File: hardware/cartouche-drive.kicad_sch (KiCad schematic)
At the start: 70 parts, among them J1 USB-C 105450-0101, J2 M.2 key M (2230), U1 JMS583, U2 TPS82130, U3 ZD25WQ16, Y1 25MHz 12pF

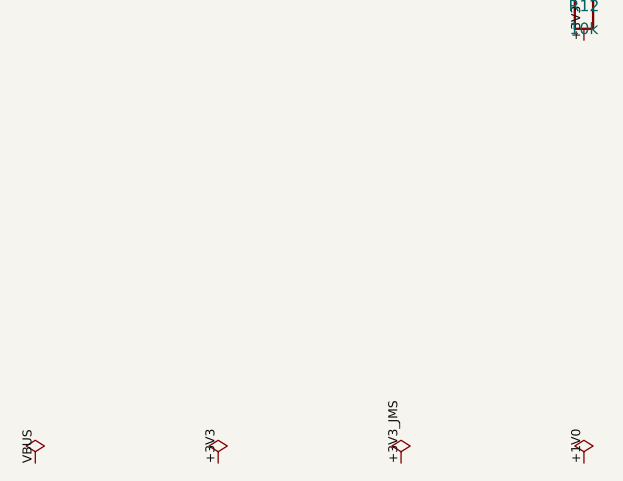
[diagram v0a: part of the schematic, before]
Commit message: PCB draft v0.1: placement, 4-layer planes, fan-out vias (not for fab)
30 x 66 mm, 4 layers: In1 solid GND, In2 split VBUS / +3V3 (SSD).
Parts placed next to the pin they serve; SSD 3.3 V buck under the SSD.
Freerouting draft: schematic parity 0, 18 unconnected left.
The 10 Gb/s USB and PCIe pairs must be re-routed as coupled pairs.

Co-Authored-By: Claude Opus 5.5 <noreply@anthropic.com>
Claude-Session: https://claude.ai/code/session_01RqDGjrUG4GdEsawKGChjmB
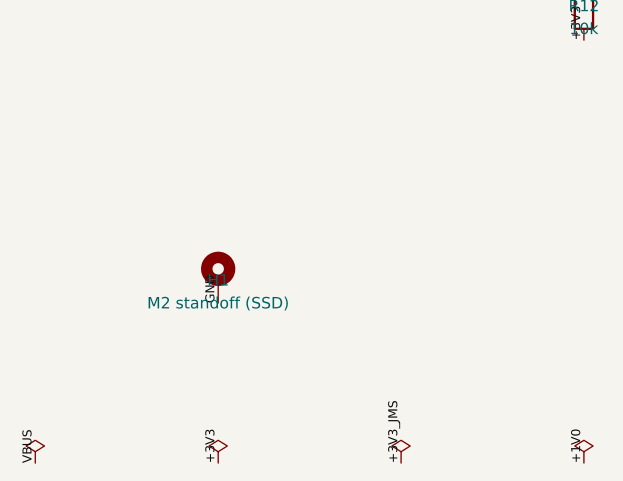
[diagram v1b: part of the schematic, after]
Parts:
- added H1: M2 standoff (SSD), MountingHole:MountingHole_2.2mm_M2_Pad_Via, symbol Mechanical:MountingHole_Pad
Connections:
- net GND: now also H1.1
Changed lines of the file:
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@@
     (pin "2")
     (instances (project "cartouche-drive" (path "/d24663b6-b77d-57d9-a649-cdccb3ccec1d" (reference "C46") (unit 1)))))
+  (symbol (lib_id "Mechanical:MountingHole_Pad") (at 59.69 330.2 0) (unit 1) (exclude_from_sim no) (in_bom no) (on_board yes) (dnp no)
+    (property "Reference" "H1" (at 59.69 330.2 0) (effects (font (size 1.27 1.27))))
+    (property "Value" "M2 standoff (SSD)" (at 59.69 332.74 0) (effects (font (size 1.27 1.27))))
+    (property "Footprint" "MountingHole:MountingHole_2.2mm_M2_Pad_Via" (at 59.69 335.28 0) (effects (font (size 1.27 1.27)) (hide yes)))
+    (property "Datasheet" "" (at 59.69 337.82 0) (effects (font (size 1.27 1.27)) (hide yes)))
+    (property "LCSC" "" (at 59.69 340.36 0) (effects (font (size 1.27 1.27)) (hide yes)))
+    (pin "1")
+    (instances (project "cartouche-drive" (path "/d24663b6-b77d-57d9-a649-cdccb3ccec1d" (reference "H1") (unit 1)))))
   (symbol (lib_id "power:PWR_FLAG") (at 39.37 350.52 0) (unit 1) (exclude_from_sim no) (in_bom no) (on_board no) (dnp no)
     (property "Reference" "#FLG1" (at 39.37 350.52 0) (effects (font (size 1.27 1.27)) (hide yes)))
@@
   (label "+3V3" (at 389.89 106.68 90) (effects (font (size 1.0 1.0)) (justify left bottom)))
   (label "GND" (at 389.89 114.3 270) (effects (font (size 1.0 1.0)) (justify left bottom)))
+  (label "GND" (at 59.69 332.74 270) (effects (font (size 1.0 1.0)) (justify left bottom)))
   (label "VBUS" (at 39.37 350.52 270) (effects (font (size 1.0 1.0)) (justify left bottom)))
   (label "+3V3" (at 59.69 350.52 270) (effects (font (size 1.0 1.0)) (justify left bottom)))

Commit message: PCB v0.2 WIP: fix PCIe TX/RX to M.2, new layout, scripted PCIe pairs
Schematic fix: M.2 PCIe pins are named from the host side (PET = host TX).
Our TX now goes through the 220 nF caps to PET0/PET1, RX comes from PER0/PER1.

New 36 x 46 mm layout: JMS583 under the SSD, its PCIe side facing the
socket's PCIe pins in the same order; USB-C on the left edge.
The 5 PCIe pairs are routed by the script (straight, one jog, caps staggered),
1.0 V and REXT pins on that side escape to vias inside the pin ring.
Still to do: USB 3.2 pairs (B-row vias between the two rows), power pours.
Not for fabrication yet.

Co-Authored-By: Claude Opus 5.5 <noreply@anthropic.com>
Claude-Session: https://claude.ai/code/session_01RqDGjrUG4GdEsawKGChjmB
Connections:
- net PCIE_RXN0: now also J2.41; no longer J2.47
- net PCIE_RXN1: now also J2.29; no longer J2.35
- net PCIE_RXP0: now also J2.43; no longer J2.49
- net PCIE_RXP1: now also J2.31; no longer J2.37
- net PCIE_TXN0_M2: now also J2.47; no longer J2.41
- net PCIE_TXN1_M2: now also J2.35; no longer J2.29
- net PCIE_TXP0_M2: now also J2.49; no longer J2.43
- net PCIE_TXP1_M2: now also J2.37; no longer J2.31
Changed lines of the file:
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@@
   (label "REFCLK_N" (at 322.58 168.91 180) (effects (font (size 1.0 1.0)) (justify right bottom)))
   (label "GND" (at 322.58 166.37 180) (effects (font (size 1.0 1.0)) (justify right bottom)))
-  (label "PCIE_RXP0" (at 322.58 163.83 180) (effects (font (size 1.0 1.0)) (justify right bottom)))
-  (label "PCIE_RXN0" (at 322.58 161.29 180) (effects (font (size 1.0 1.0)) (justify right bottom)))
+  (label "PCIE_TXP0_M2" (at 322.58 163.83 180) (effects (font (size 1.0 1.0)) (justify right bottom)))
+  (label "PCIE_TXN0_M2" (at 322.58 161.29 180) (effects (font (size 1.0 1.0)) (justify right bottom)))
   (label "GND" (at 322.58 158.75 180) (effects (font (size 1.0 1.0)) (justify right bottom)))
-  (label "PCIE_TXP0_M2" (at 322.58 156.21 180) (effects (font (size 1.0 1.0)) (justify right bottom)))
-  (label "PCIE_TXN0_M2" (at 322.58 153.67 180) (effects (font (size 1.0 1.0)) (justify right bottom)))
+  (label "PCIE_RXP0" (at 322.58 156.21 180) (effects (font (size 1.0 1.0)) (justify right bottom)))
+  (label "PCIE_RXN0" (at 322.58 153.67 180) (effects (font (size 1.0 1.0)) (justify right bottom)))
   (label "GND" (at 322.58 151.13 180) (effects (font (size 1.0 1.0)) (justify right bottom)))
-  (label "PCIE_RXP1" (at 322.58 148.59 180) (effects (font (size 1.0 1.0)) (justify right bottom)))
-  (label "PCIE_RXN1" (at 322.58 146.05 180) (effects (font (size 1.0 1.0)) (justify right bottom)))
+  (label "PCIE_TXP1_M2" (at 322.58 148.59 180) (effects (font (size 1.0 1.0)) (justify right bottom)))
+  (label "PCIE_TXN1_M2" (at 322.58 146.05 180) (effects (font (size 1.0 1.0)) (justify right bottom)))
   (label "GND" (at 322.58 143.51 180) (effects (font (size 1.0 1.0)) (justify right bottom)))
-  (label "PCIE_TXP1_M2" (at 322.58 140.97 180) (effects (font (size 1.0 1.0)) (justify right bottom)))
-  (label "PCIE_TXN1_M2" (at 322.58 138.43 180) (effects (font (size 1.0 1.0)) (justify right bottom)))
+  (label "PCIE_RXP1" (at 322.58 140.97 180) (effects (font (size 1.0 1.0)) (justify right bottom)))
+  (label "PCIE_RXN1" (at 322.58 138.43 180) (effects (font (size 1.0 1.0)) (justify right bottom)))
   (label "PERST" (at 337.82 165.1 0) (effects (font (size 1.0 1.0)) (justify left bottom)))
   (label "GND" (at 322.58 135.89 180) (effects (font (size 1.0 1.0)) (justify right bottom)))

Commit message: PCB v0.3 WIP: scripted USB 3.2 pairs, B.Cu power pours, 0201 USB caps
USB-C B row reached through vias placed between the two pad rows.
TX1/RX2 straight on F.Cu; TX2/RX1 cross on B.Cu over the In2 ground plane.
In1 and In2 are both ground; VBUS and +3V3 are pours on B.Cu, split between
the regulator's VIN and VOUT pads. USB SuperSpeed caps moved to 0201.
DRC: 0 schematic mismatch, 0 clearance on the pairs, 4 unconnected left.
Not ready for fabrication.

Co-Authored-By: Claude Opus 5.5 <noreply@anthropic.com>
Claude-Session: https://claude.ai/code/session_01RqDGjrUG4GdEsawKGChjmB
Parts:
- C1, C2, C3, C4: footprint Capacitor_SMD:C_0402_1005Metric -> Capacitor_SMD:C_0201_0603Metric; LCSC C1525 -> (none)
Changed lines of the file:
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@@
     (property "Reference" "C1" (at 110.49 95.25 0) (effects (font (size 1.27 1.27))))
     (property "Value" "100nF" (at 110.49 97.79 0) (effects (font (size 1.27 1.27))))
-    (property "Footprint" "Capacitor_SMD:C_0402_1005Metric" (at 110.49 100.33 0) (effects (font (size 1.27 1.27)) (hide yes)))
+    (property "Footprint" "Capacitor_SMD:C_0201_0603Metric" (at 110.49 100.33 0) (effects (font (size 1.27 1.27)) (hide yes)))
     (property "Datasheet" "" (at 110.49 102.87 0) (effects (font (size 1.27 1.27)) (hide yes)))
-    (property "LCSC" "C1525" (at 110.49 105.41 0) (effects (font (size 1.27 1.27)) (hide yes)))
+    (property "LCSC" "" (at 110.49 105.41 0) (effects (font (size 1.27 1.27)) (hide yes)))
     (pin "1")
     (pin "2")
@@
     (property "Reference" "C2" (at 110.49 105.41 0) (effects (font (size 1.27 1.27))))
     (property "Value" "100nF" (at 110.49 107.95 0) (effects (font (size 1.27 1.27))))
-    (property "Footprint" "Capacitor_SMD:C_0402_1005Metric" (at 110.49 110.49 0) (effects (font (size 1.27 1.27)) (hide yes)))
+    (property "Footprint" "Capacitor_SMD:C_0201_0603Metric" (at 110.49 110.49 0) (effects (font (size 1.27 1.27)) (hide yes)))
     (property "Datasheet" "" (at 110.49 113.03 0) (effects (font (size 1.27 1.27)) (hide yes)))
-    (property "LCSC" "C1525" (at 110.49 115.57 0) (effects (font (size 1.27 1.27)) (hide yes)))
+    (property "LCSC" "" (at 110.49 115.57 0) (effects (font (size 1.27 1.27)) (hide yes)))
     (pin "1")
     (pin "2")
@@
     (property "Reference" "C3" (at 110.49 115.57 0) (effects (font (size 1.27 1.27))))
     (property "Value" "100nF" (at 110.49 118.11 0) (effects (font (size 1.27 1.27))))
-    (property "Footprint" "Capacitor_SMD:C_0402_1005Metric" (at 110.49 120.64999999999999 0) (effects (font (size 1.27 1.27)) (hide yes)))
+    (property "Footprint" "Capacitor_SMD:C_0201_0603Metric" (at 110.49 120.64999999999999 0) (effects (font (size 1.27 1.27)) (hide yes)))
     (property "Datasheet" "" (at 110.49 123.19 0) (effects (font (size 1.27 1.27)) (hide yes)))
-    (property "LCSC" "C1525" (at 110.49 125.72999999999999 0) (effects (font (size 1.27 1.27)) (hide yes)))
+    (property "LCSC" "" (at 110.49 125.72999999999999 0) (effects (font (size 1.27 1.27)) (hide yes)))
     (pin "1")
     (pin "2")
@@
     (property "Reference" "C4" (at 110.49 124.46 0) (effects (font (size 1.27 1.27))))
     (property "Value" "100nF" (at 110.49 127.0 0) (effects (font (size 1.27 1.27))))
-    (property "Footprint" "Capacitor_SMD:C_0402_1005Metric" (at 110.49 129.54 0) (effects (font (size 1.27 1.27)) (hide yes)))
+    (property "Footprint" "Capacitor_SMD:C_0201_0603Metric" (at 110.49 129.54 0) (effects (font (size 1.27 1.27)) (hide yes)))
     (property "Datasheet" "" (at 110.49 132.07999999999998 0) (effects (font (size 1.27 1.27)) (hide yes)))
-    (property "LCSC" "C1525" (at 110.49 134.62 0) (effects (font (size 1.27 1.27)) (hide yes)))
+    (property "LCSC" "" (at 110.49 134.62 0) (effects (font (size 1.27 1.27)) (hide yes)))
     (pin "1")
     (pin "2")

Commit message: PCB v0.4: fab files, stitching, 1.0 V island, tighter USB pairs
- USB pairs 0.2/0.1 mm, GND stitching vias, +1V0 island on In2
- 0 unconnected, 0 parity errors in DRC
- hardware/fab: Gerbers + drill (zip), JLCPCB BOM and CPL (tools/jlc_files.py)
- LCSC: C1-C4 C76934, L1 C383386

Co-Authored-By: Claude Opus 5.5 <noreply@anthropic.com>
Claude-Session: https://claude.ai/code/session_01RqDGjrUG4GdEsawKGChjmB
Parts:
- C1, C2, C3, C4: LCSC (none) -> C76934
- L1: LCSC (none) -> C383386
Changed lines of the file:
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@@
     (property "Footprint" "Capacitor_SMD:C_0201_0603Metric" (at 110.49 100.33 0) (effects (font (size 1.27 1.27)) (hide yes)))
     (property "Datasheet" "" (at 110.49 102.87 0) (effects (font (size 1.27 1.27)) (hide yes)))
-    (property "LCSC" "" (at 110.49 105.41 0) (effects (font (size 1.27 1.27)) (hide yes)))
+    (property "LCSC" "C76934" (at 110.49 105.41 0) (effects (font (size 1.27 1.27)) (hide yes)))
     (pin "1")
     (pin "2")
@@
     (property "Footprint" "Capacitor_SMD:C_0201_0603Metric" (at 110.49 110.49 0) (effects (font (size 1.27 1.27)) (hide yes)))
     (property "Datasheet" "" (at 110.49 113.03 0) (effects (font (size 1.27 1.27)) (hide yes)))
-    (property "LCSC" "" (at 110.49 115.57 0) (effects (font (size 1.27 1.27)) (hide yes)))
+    (property "LCSC" "C76934" (at 110.49 115.57 0) (effects (font (size 1.27 1.27)) (hide yes)))
     (pin "1")
     (pin "2")
@@
     (property "Footprint" "Capacitor_SMD:C_0201_0603Metric" (at 110.49 120.64999999999999 0) (effects (font (size 1.27 1.27)) (hide yes)))
     (property "Datasheet" "" (at 110.49 123.19 0) (effects (font (size 1.27 1.27)) (hide yes)))
-    (property "LCSC" "" (at 110.49 125.72999999999999 0) (effects (font (size 1.27 1.27)) (hide yes)))
+    (property "LCSC" "C76934" (at 110.49 125.72999999999999 0) (effects (font (size 1.27 1.27)) (hide yes)))
     (pin "1")
     (pin "2")
@@
     (property "Footprint" "Capacitor_SMD:C_0201_0603Metric" (at 110.49 129.54 0) (effects (font (size 1.27 1.27)) (hide yes)))
     (property "Datasheet" "" (at 110.49 132.07999999999998 0) (effects (font (size 1.27 1.27)) (hide yes)))
-    (property "LCSC" "" (at 110.49 134.62 0) (effects (font (size 1.27 1.27)) (hide yes)))
+    (property "LCSC" "C76934" (at 110.49 134.62 0) (effects (font (size 1.27 1.27)) (hide yes)))
     (pin "1")
     (pin "2")
@@
     (property "Footprint" "Inductor_SMD:L_1008_2520Metric" (at 149.86 64.77 0) (effects (font (size 1.27 1.27)) (hide yes)))
     (property "Datasheet" "" (at 149.86 67.31 0) (effects (font (size 1.27 1.27)) (hide yes)))
-    (property "LCSC" "" (at 149.86 69.85 0) (effects (font (size 1.27 1.27)) (hide yes)))
+    (property "LCSC" "C383386" (at 149.86 69.85 0) (effects (font (size 1.27 1.27)) (hide yes)))
     (pin "1")
     (pin "2")
